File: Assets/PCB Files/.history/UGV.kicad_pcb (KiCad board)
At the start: 2 copper layers, 120.6 x 156.5 mm, 96 parts, among them J13 USB3_A, J15 Screw_Terminal_01x12, J16 Screw_Terminal_01x12, J17 Screw_Terminal_01x12, J18 Screw_Terminal_01x12, Q1 AO3400A, Q2 AO3400A, Q3 AO3400A, U2 LMR33630ADDA, U3 SN74LVC8T245, U4 Teensy4.1, U5 SN74LVC8T245

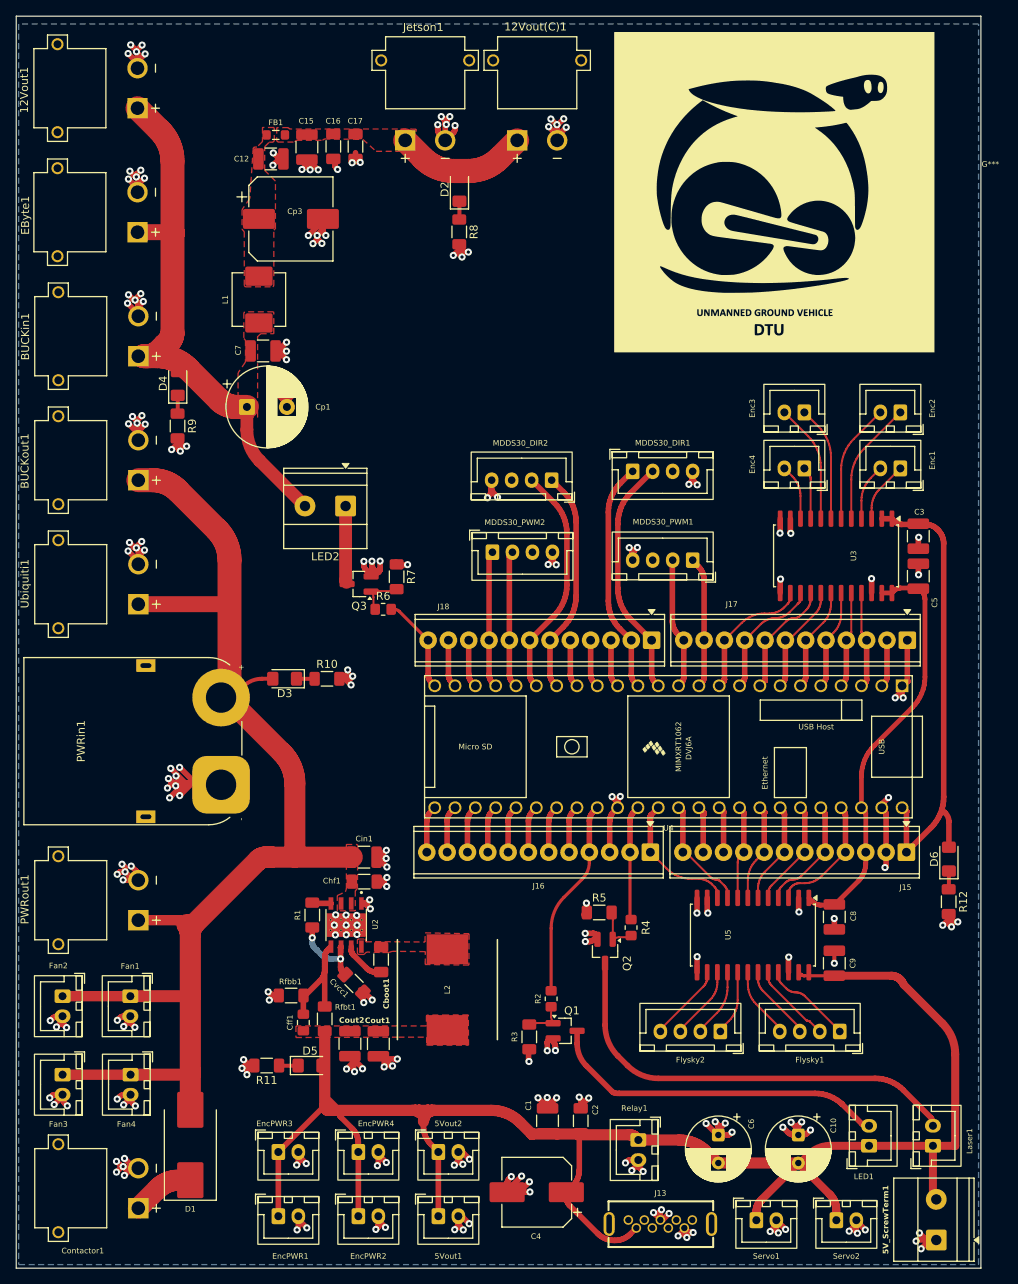
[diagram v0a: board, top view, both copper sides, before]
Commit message: Routing changes in the LMR IC and a few small changes too
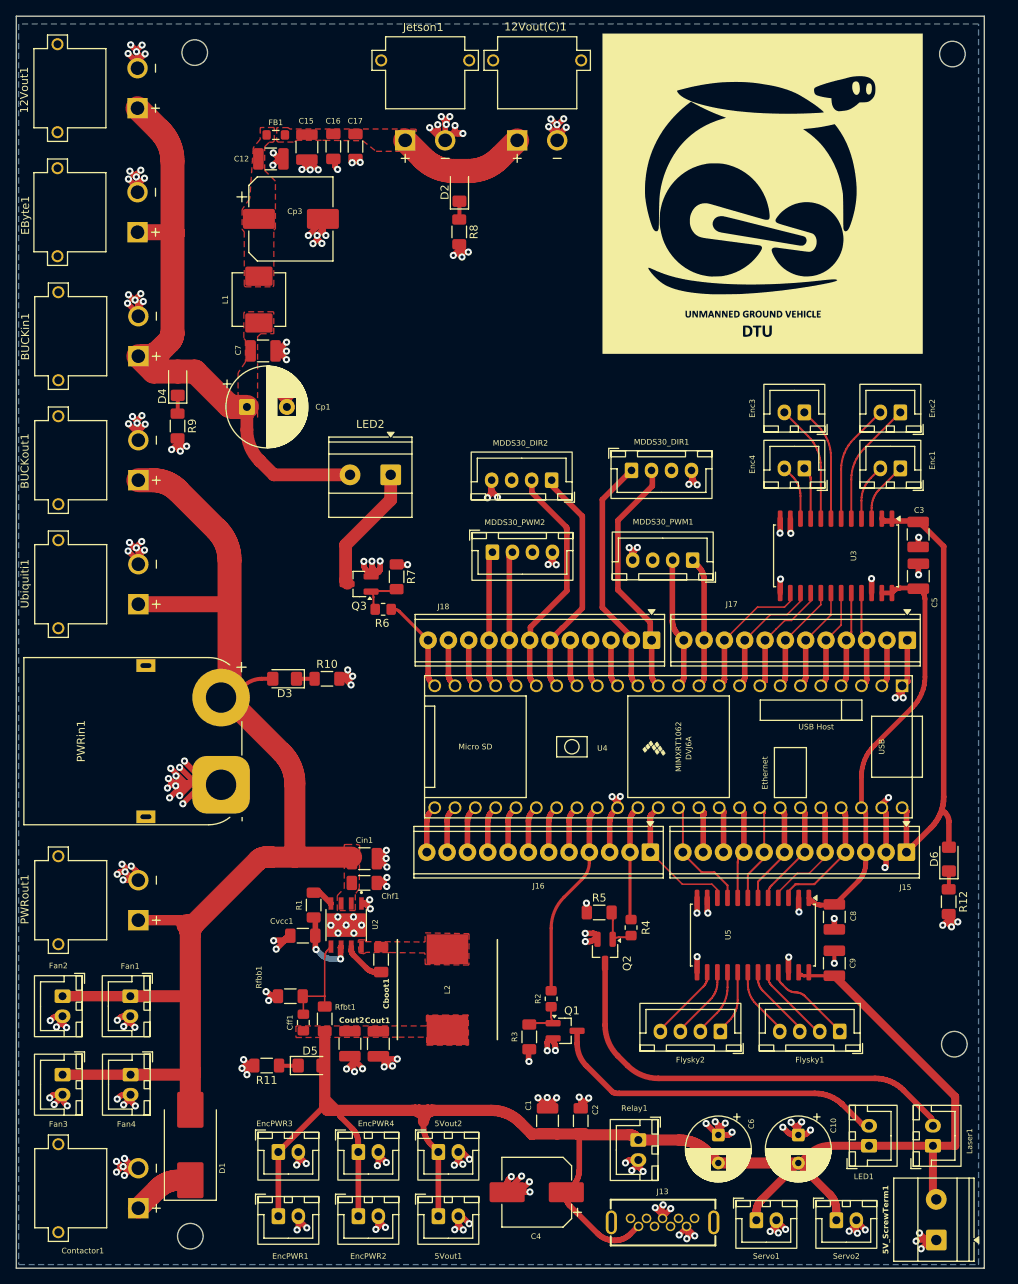
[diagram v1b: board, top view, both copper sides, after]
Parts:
- added REF**: MountingHole_3.2mm_M3, MountingHole:MountingHole_3.2mm_M3, F.Cu at (117.8, 5.73)
- added REF**: MountingHole_3.2mm_M3, MountingHole:MountingHole_3.2mm_M3, F.Cu at (22.5, 153.5)
- added REF**: MountingHole_3.2mm_M3, MountingHole:MountingHole_3.2mm_M3, F.Cu at (23.0, 5.55)
- added REF**: MountingHole_3.2mm_M3, MountingHole:MountingHole_3.2mm_M3, F.Cu at (118.0, 129.5)
- PWRin1: footprint Connector_AMASS:AMASS_XT90PW-M_1x02_P10.90mm_Horizontal -> UGV_Custom:AMASS_XT90PW-M_1x02_P10.90mm_Horizontal
- moved Cvcc1 8.75 mm to (36.6, 115.9), turned to 180 degrees
- moved LED2 6.85 mm to (47.5, 58.3)
- moved G*** 1.48 mm to (94.0, 23.2)
- moved R1 1.26 mm to (37.9, 112.1)
- moved J13 0.34 mm to (81.5, 151.8)
- moved C3 0.22 mm to (113.5, 65.8)
- moved Cin1 0.19 mm to (44.3, 106.3)
- moved MDDS30_DIR1 0.19 mm to (77.6, 57.8)
- moved Chf1 0.16 mm to (44.2, 109.3)
- moved Rfbb1 0.13 mm to (35.0, 123.5)
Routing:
- net GND: track 352.4 -> 335.8 mm, vias 213 -> 215
- net /Vout: track 230.4 -> 223.3 mm
- net Net-(D4-A): track 69.6 -> 76.4 mm
- net /M1: track 9.73 -> 16.0 mm
- net Net-(U2-FB): track 15.9 -> 12.7 mm
- net Net-(D1-A): track 164.5 -> 161.6 mm
- net Net-(U2-VCC): track 10.9 -> 8.76 mm
- net Net-(U5-B3): track 9.45 -> 7.91 mm
- net /22: track 14.4 -> 13.0 mm
- net Net-(U2-PG): track 1.60 -> 2.99 mm
- net /19: track 12.2 -> 10.9 mm
- net /3V3: track 58.7 -> 57.4 mm
- net /21: track 13.3 -> 12.1 mm
- net Net-(U5-B8): track 9.75 -> 8.59 mm
- net /26: track 28.1 -> 29.3 mm
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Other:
- board size 120.6 x 156.5 mm -> 121 x 156.5 mm
- board text added: "Rfbb1"
